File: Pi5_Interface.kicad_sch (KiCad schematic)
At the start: 7 parts, among them J13 Pi 5 UART, J14 Pi 5 power

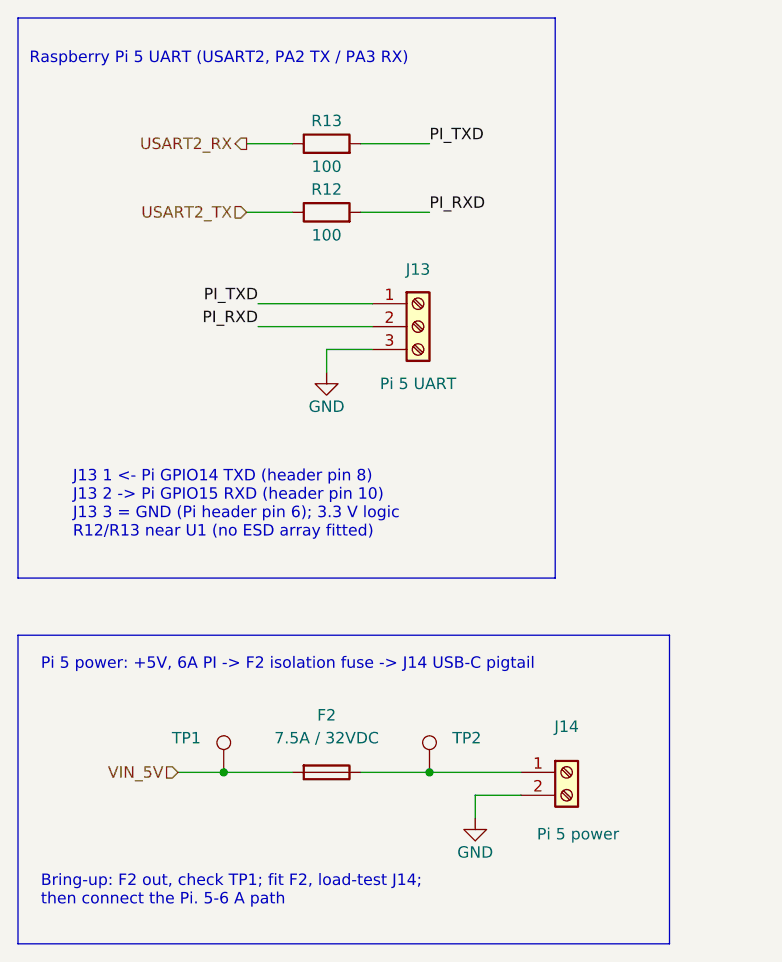
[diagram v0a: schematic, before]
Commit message: Rename power nets, add mounting holes, retitle sheet 1, clear ERC
Power nets, no commas, named by function:
- "+5V, 2A" -> +5V_SYS, "+5V, 6A PI" -> +5V_PI, "+5V, 6A AUX" -> +5V_AUX
Buck sheets renamed to Buck 5V SYS / Buck 5V PI / Buck 5V AUX. Notes,
descriptions, README and docs updated.

Mechanical and title:
- H1-H4: M3 mounting holes, 3.2 mm plated, isolated (no net), not in BOM
- Sheet 1 title: "Delivery Robot Main Board"

ERC, now 0 errors and 0 warnings (was 4 errors, 15 warnings):
- PWR_FLAGs on +12V (after F1), GND (at J2), +3.3VA (after FB2) and
  +5V_SYS (after the TPS54202's L1)
- TPSM63606 symbol pin types set (VOUT power out, FB/EN input, VIN/
  VLDOIN/GND power in, PG open collector, others passive) in both buck
  sheets and libs/TPSM63606RDLR.kicad_sym
- U1 STM32F091RCTx and Y3 Crystal_GND24 moved to a new
  libs/project_symbols.kicad_sym holding the versions this design uses
  (the current KiCad library moved their pins); libs/TPS54202DDCR made
  to match the schematic's U3
Connectivity unchanged: same 108 nets and pins.

Co-Authored-By: Claude Opus 5.5 <noreply@anthropic.com>
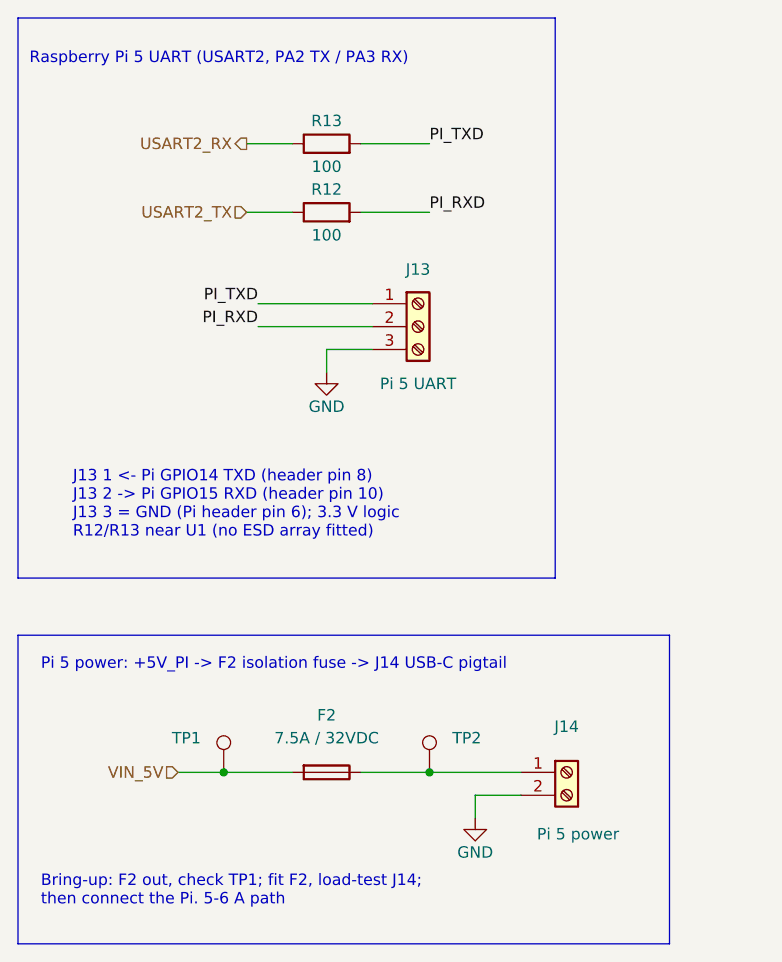
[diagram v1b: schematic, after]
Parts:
- TP1: value +5V, 6A PI -> +5V_PI
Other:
- note added: "Pi 5 power: +5V_PI -> F2 isolation fuse -> J14 USB-C pigtail"
- note removed: "Pi 5 power: +5V, 6A PI -> F2 isolation fuse -> J14 USB-C pigtail"
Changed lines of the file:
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@@
 		)
 	)
-	(text "Pi 5 power: +5V, 6A PI -> F2 isolation fuse -> J14 USB-C pigtail"
+	(text "Pi 5 power: +5V_PI -> F2 isolation fuse -> J14 USB-C pigtail"
 		(exclude_from_sim no)
 		(at 49.53 111.76 0)
@@
 			)
 		)
-		(property "Value" "+5V, 6A PI"
+		(property "Value" "+5V_PI"
 			(at 69.85 128.27 0)
 			(hide yes)
